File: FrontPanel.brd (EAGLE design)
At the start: 100 x 61 mm, 29 parts, among them U1 TPIC6B595N, U2 TPIC6B595N, U3 TPIC6B595N, U4 TPIC6B595N, U5 TPIC6B595N, U6 TPIC6B595N

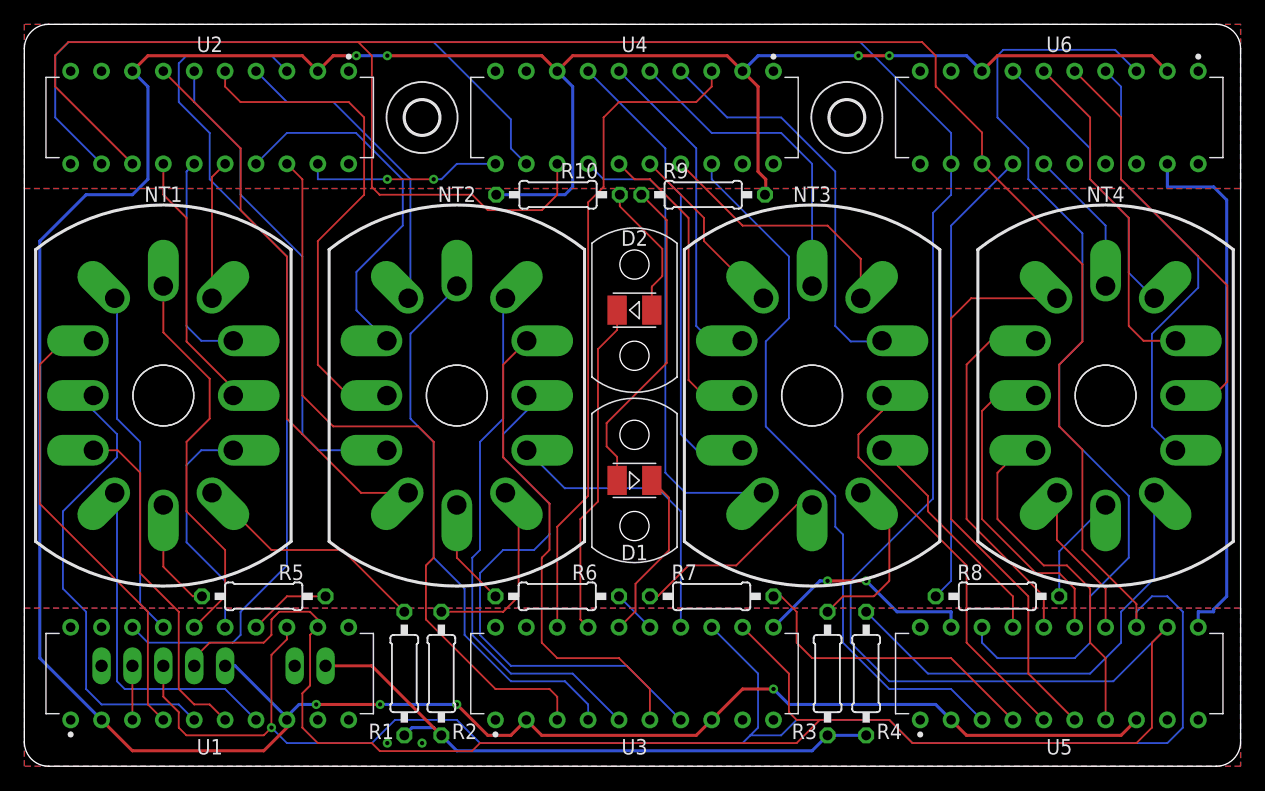
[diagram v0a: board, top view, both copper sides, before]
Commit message: added additional mounting hole
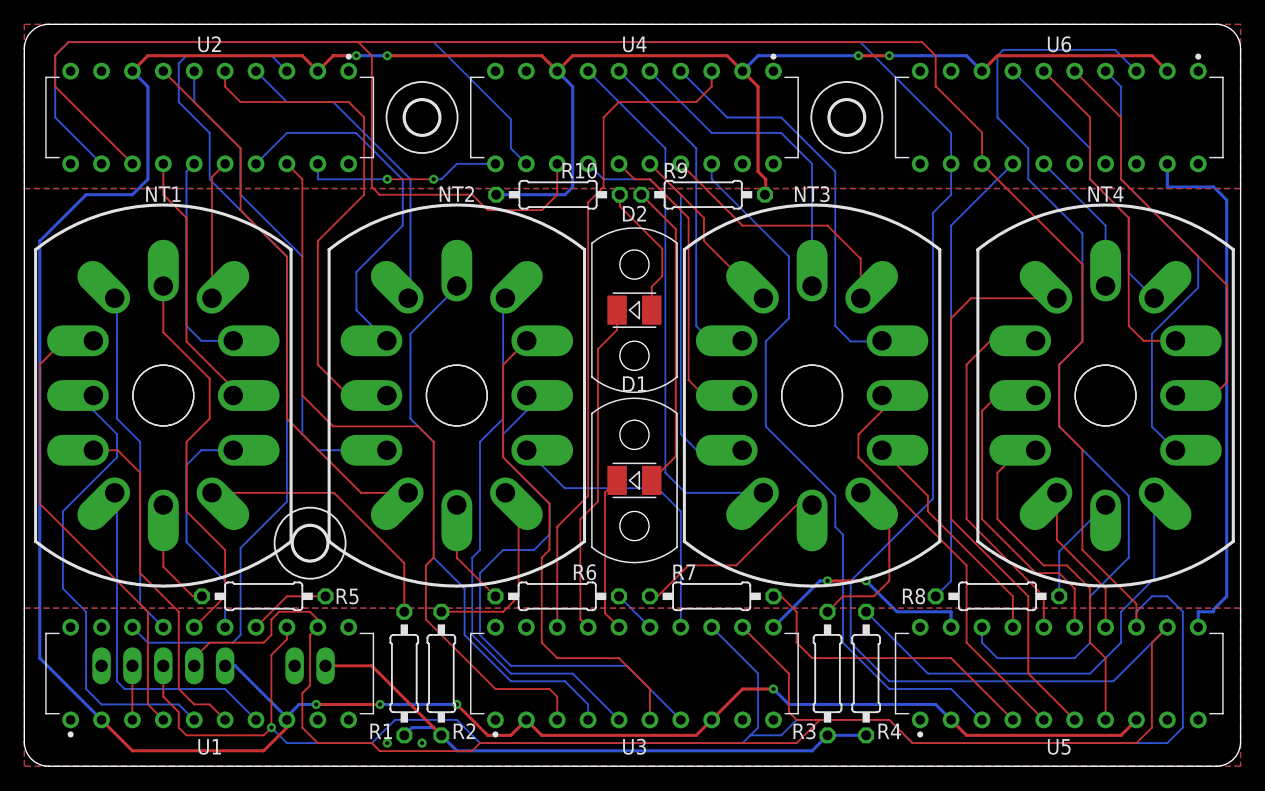
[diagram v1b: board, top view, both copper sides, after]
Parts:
- added U$3: (no value), holes:2,8
- turned D1 to 0 degrees
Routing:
- net N$49: track 19.9 -> 22.2 mm
- net LED1: track 14.4 -> 13.0 mm
- net N$66: track 26.8 -> 25.5 mm
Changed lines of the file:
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@@
 <drawing>
 <settings>
-<setting alwaysvectorfont="yes"/>
+<setting alwaysvectorfont="no"/>
 <setting verticaltext="up"/>
 </settings>
@@
 </element>
 <element name="R5" library="rcl" library_urn="urn:adsk.eagle:library:334" package="0207/10" package3d_urn="urn:adsk.eagle:package:23491/2" value="100k" x="19.685" y="13.97" smashed="yes">
-<attribute name="NAME" x="22.987" y="15.3162" size="1.27" layer="25" ratio="10" align="bottom-right"/>
+<attribute name="NAME" x="25.527" y="13.97" size="1.27" layer="25" ratio="10" align="center-left"/>
 <attribute name="SPICEPREFIX" value="R" x="38.735" y="-96.52" size="1.778" layer="27" display="off"/>
 <attribute name="VALUE" x="17.4244" y="13.335" size="1.27" layer="27" ratio="10"/>
@@
 </element>
 <element name="R8" library="rcl" library_urn="urn:adsk.eagle:library:334" package="0207/10" package3d_urn="urn:adsk.eagle:package:23491/2" value="100k" x="80.01" y="13.97" smashed="yes">
-<attribute name="NAME" x="76.708" y="15.3162" size="1.27" layer="25" ratio="10"/>
+<attribute name="NAME" x="74.168" y="13.97" size="1.27" layer="25" ratio="10" align="center-right"/>
 <attribute name="SPICEPREFIX" value="R" x="137.16" y="-96.52" size="1.778" layer="27" display="off"/>
 <attribute name="VALUE" x="77.7494" y="13.335" size="1.27" layer="27" ratio="10"/>
@@
 <element name="U$5" library="NixieClock" library_urn="urn:adsk.eagle:library:7479626" package="MENTOR-1216.1005" package3d_urn="urn:adsk.eagle:package:7524597/2" value="" x="50.165" y="37.5" smashed="yes" rot="R90"/>
 <element name="U$6" library="NixieClock" library_urn="urn:adsk.eagle:library:7479626" package="MENTOR-1216.1005" package3d_urn="urn:adsk.eagle:package:7524597/2" value="" x="50.165" y="23.5" smashed="yes" rot="R90"/>
-<element name="D1" library="Wurth_Elektronik_Optoelectronics_rev17b" library_urn="urn:adsk.eagle:library:446" package="WL-SMTW_3528" package3d_urn="urn:adsk.eagle:package:32264/1" value="" x="50.165" y="23.5" smashed="yes" rot="R180">
-<attribute name="COMPANY-URL" value="http://www.we-online.de" x="50.165" y="23.5" size="1.778" layer="27" rot="R180" display="off"/>
-<attribute name="CREATED-BY" value="Christin Otto" x="50.165" y="23.5" size="1.778" layer="27" rot="R180" display="off"/>
-<attribute name="CREATED-DATE" value="APR 2013" x="50.165" y="23.5" size="1.778" layer="27" rot="R180" display="off"/>
-<attribute name="DATASHEET-URL" value="http://katalog.we-online.de/en/led/WL-SMTW?m=t&amp;sq=smtw&amp;sp=&amp;sp=http%3A%2F%2Fwww.we-online.de%2Fweb%2Fen%2Felectronic_components%2Fsearchpage_PBS.php%3Fsearch%3Dsmtw" x="50.165" y="23.5" size="1.778" layer="27" rot="R180" display="off"/>
-<attribute name="MANUFACTURER" value="Würth Elektronik eiSos GmbH" x="50.165" y="23.5" size="1.778" layer="27" rot="R180" display="off"/>
-<attribute name="NAME" x="50.165" y="18.2095" size="1.27" layer="25" align="top-center"/>
-<attribute name="VALUE" x="52.305" y="26.31" size="0.8128" layer="27" rot="R180"/>
+<element name="D1" library="Wurth_Elektronik_Optoelectronics_rev17b" library_urn="urn:adsk.eagle:library:446" package="WL-SMTW_3528" package3d_urn="urn:adsk.eagle:package:32264/1" value="" x="50.165" y="23.5" smashed="yes">
+<attribute name="COMPANY-URL" value="http://www.we-online.de" x="50.165" y="23.5" size="1.778" layer="27" display="off"/>
+<attribute name="CREATED-BY" value="Christin Otto" x="50.165" y="23.5" size="1.778" layer="27" display="off"/>
+<attribute name="CREATED-DATE" value="APR 2013" x="50.165" y="23.5" size="1.778" layer="27" display="off"/>
+<attribute name="DATASHEET-URL" value="http://katalog.we-online.de/en/led/WL-SMTW?m=t&amp;sq=smtw&amp;sp=&amp;sp=http%3A%2F%2Fwww.we-online.de%2Fweb%2Fen%2Felectronic_components%2Fsearchpage_PBS.php%3Fsearch%3Dsmtw" x="50.165" y="23.5" size="1.778" layer="27" display="off"/>
+<attribute name="MANUFACTURER" value="Würth Elektronik eiSos GmbH" x="50.165" y="23.5" size="1.778" layer="27" display="off"/>
+<attribute name="NAME" x="50.165" y="30.7905" size="1.27" layer="25" rot="R180" align="top-center"/>
+<attribute name="VALUE" x="48.025" y="20.69" size="0.8128" layer="27"/>
 </element>
 <element name="D2" library="Wurth_Elektronik_Optoelectronics_rev17b" library_urn="urn:adsk.eagle:library:446" package="WL-SMTW_3528" package3d_urn="urn:adsk.eagle:package:32264/1" value="" x="50.165" y="37.5" smashed="yes">
@@
 <attribute name="DATASHEET-URL" value="http://katalog.we-online.de/en/led/WL-SMTW?m=t&amp;sq=smtw&amp;sp=&amp;sp=http%3A%2F%2Fwww.we-online.de%2Fweb%2Fen%2Felectronic_components%2Fsearchpage_PBS.php%3Fsearch%3Dsmtw" x="50.165" y="37.5" size="1.778" layer="27" display="off"/>
 <attribute name="MANUFACTURER" value="Würth Elektronik eiSos GmbH" x="50.165" y="37.5" size="1.778" layer="27" display="off"/>
-<attribute name="NAME" x="50.165" y="42.7905" size="1.27" layer="25" align="bottom-center"/>
+<attribute name="NAME" x="50.165" y="44.7905" size="1.27" layer="25" align="bottom-center"/>
 <attribute name="VALUE" x="48.025" y="34.69" size="0.8128" layer="27"/>
 </element>
+<element name="U$3" library="holes" library_urn="urn:adsk.eagle:library:237" package="2,8" package3d_urn="urn:adsk.eagle:package:14271/1" value="" x="23.495" y="18.34" smashed="yes"/>
 </elements>
 <signals>
@@
 <contactref element="U3" pad="16"/>
 <contactref element="D1" pad="1"/>
-<wire x1="50.25" y1="12.75" x2="50.25" y2="15" width="0.1524" layer="1"/>
-<wire x1="50.25" y1="15" x2="53" y2="17.75" width="0.1524" layer="1"/>
-<wire x1="53" y1="22.09" x2="51.59" y2="23.5" width="0.1524" layer="1"/>
-<wire x1="50.25" y1="12.75" x2="48.895" y2="11.395" width="0.1524" layer="1"/>
-<wire x1="48.895" y1="11.43" x2="48.895" y2="11.395" width="0.1524" layer="1"/>
-<wire x1="53" y1="17.75" x2="53" y2="22.09" width="0.1524" layer="1"/>
+<wire x1="48.74" y1="23.5" x2="47.74" y2="22.5" width="0.1524" layer="1"/>
+<wire x1="47.74" y1="22.5" x2="47.74" y2="12.585" width="0.1524" layer="1"/>
+<wire x1="47.74" y1="12.585" x2="48.895" y2="11.43" width="0.1524" layer="1"/>
 </signal>
 <signal name="LED2">
@@
 <contactref element="NT1" pad="A"/>
 <contactref element="R1" pad="1"/>
-<wire x1="31.242" y1="12.7" x2="26.162" y2="17.78" width="0.1524" layer="1"/>
-<wire x1="20.32" y1="17.78" x2="15.62" y2="22.48" width="0.1524" layer="1"/>
-<wire x1="15.62" y1="22.48" x2="15.43" y2="22.48" width="0.1524" layer="1"/>
-<wire x1="26.162" y1="17.78" x2="20.32" y2="17.78" width="0.1524" layer="1"/>
+<wire x1="31.242" y1="12.7" x2="31.242" y2="16.7" width="0.1524" layer="1"/>
+<wire x1="31.242" y1="16.7" x2="25.462" y2="22.48" width="0.1524" layer="1"/>
+<wire x1="25.462" y1="22.48" x2="15.43" y2="22.48" width="0.1524" layer="1"/>
 </signal>
 <signal name="N$50">
@@
 <contactref element="U2" pad="3"/>
 <contactref element="U1" pad="18"/>
-<wire x1="21.59" y1="16.51" x2="17.78" y2="12.7" width="0.1524" layer="16"/>
+<wire x1="21.59" y1="21.76" x2="17.78" y2="17.95" width="0.1524" layer="16"/>
 <wire x1="21.59" y1="41.91" x2="15.24" y2="48.26" width="0.1524" layer="16"/>
 <wire x1="15.24" y1="48.26" x2="15.24" y2="52.07" width="0.1524" layer="16"/>
 <wire x1="12.7" y1="54.61" x2="15.24" y2="52.07" width="0.1524" layer="16"/>
 <wire x1="21.59" y1="57.15" x2="20.32" y2="58.42" width="0.1524" layer="16"/>
-<wire x1="21.59" y1="16.51" x2="21.59" y2="41.91" width="0.1524" layer="16"/>
+<wire x1="21.59" y1="21.76" x2="21.59" y2="41.91" width="0.1524" layer="16"/>
 <wire x1="13.335" y1="58.42" x2="12.7" y2="57.785" width="0.1524" layer="16"/>
 <wire x1="12.7" y1="57.785" x2="12.7" y2="54.61" width="0.1524" layer="16"/>
@@
 <wire x1="17.78" y1="10.795" x2="17.145" y2="10.16" width="0.1524" layer="16"/>
 <wire x1="10.16" y1="10.16" x2="8.89" y2="11.43" width="0.1524" layer="16"/>
-<wire x1="17.78" y1="12.7" x2="17.78" y2="10.795" width="0.1524" layer="16"/>
+<wire x1="17.78" y1="17.95" x2="17.78" y2="10.795" width="0.1524" layer="16"/>
 <wire x1="17.145" y1="10.16" x2="10.16" y2="10.16" width="0.1524" layer="16"/>
 </signal>
@@
 <contactref element="R9" pad="1"/>
 <contactref element="D1" pad="2"/>
-<wire x1="48.74" y1="23.5" x2="48.74" y2="25.4333375" width="0.1524" layer="1"/>
-<wire x1="48.74" y1="25.4333375" x2="47.8728" y2="26.3005375" width="0.1524" layer="1"/>
-<wire x1="47.8728" y1="26.3005375" x2="47.8728" y2="28.2161375" width="0.1524" layer="1"/>
-<wire x1="52.8128" y1="44.9122" x2="52.8128" y2="33.1561375" width="0.1524" layer="1"/>
-<wire x1="50.735" y1="46.99" x2="52.8128" y2="44.9122" width="0.1524" layer="1"/>
-<wire x1="52.8128" y1="33.1561375" x2="47.8728" y2="28.2161375" width="0.1524" layer="1"/>
+<wire x1="53.5628" y1="44.1622" x2="53.5628" y2="25.4728" width="0.1524" layer="1"/>
+<wire x1="51.59" y1="23.5" x2="53.5628" y2="25.4728" width="0.1524" layer="1"/>
+<wire x1="50.735" y1="46.99" x2="53.5628" y2="44.1622" width="0.1524" layer="1"/>
 </signal>
 <signal name="N$67">

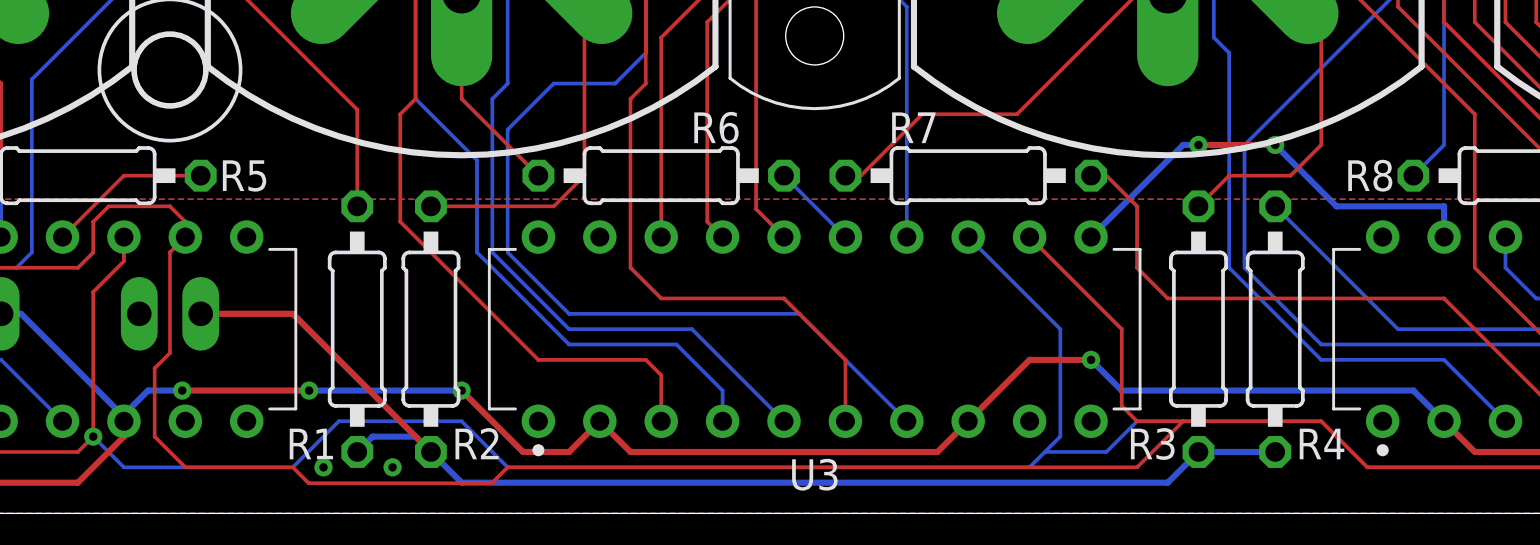
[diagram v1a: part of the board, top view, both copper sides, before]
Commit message: fixed airwire in front panel and updated panel
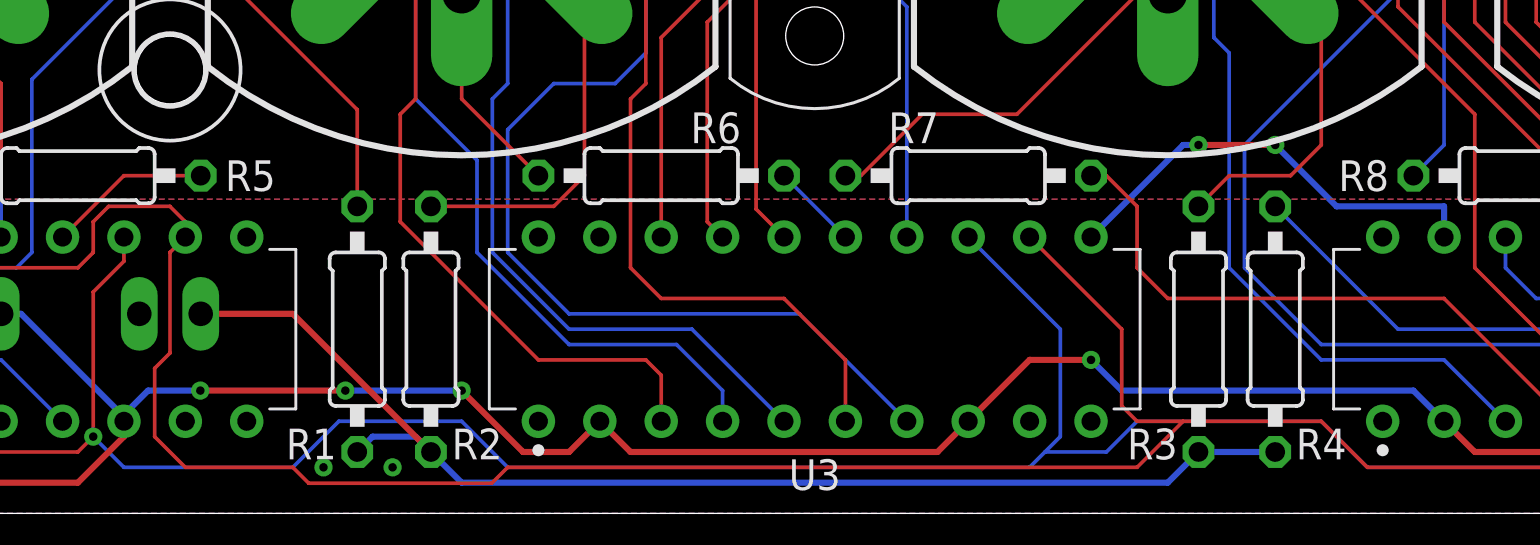
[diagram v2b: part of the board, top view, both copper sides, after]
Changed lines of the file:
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@@
 <drawing>
 <settings>
-<setting alwaysvectorfont="no"/>
+<setting alwaysvectorfont="yes"/>
 <setting verticaltext="up"/>
 </settings>
@@
 </element>
 <element name="R5" library="rcl" library_urn="urn:adsk.eagle:library:334" package="0207/10" package3d_urn="urn:adsk.eagle:package:23491/2" value="100k" x="19.685" y="13.97" smashed="yes">
-<attribute name="NAME" x="25.527" y="13.97" size="1.27" layer="25" ratio="10" align="center-left"/>
+<attribute name="NAME" x="25.777" y="13.97" size="1.27" layer="25" ratio="10" align="center-left"/>
 <attribute name="SPICEPREFIX" value="R" x="38.735" y="-96.52" size="1.778" layer="27" display="off"/>
 <attribute name="VALUE" x="17.4244" y="13.335" size="1.27" layer="27" ratio="10"/>
@@
 </element>
 <element name="R8" library="rcl" library_urn="urn:adsk.eagle:library:334" package="0207/10" package3d_urn="urn:adsk.eagle:package:23491/2" value="100k" x="80.01" y="13.97" smashed="yes">
-<attribute name="NAME" x="74.168" y="13.97" size="1.27" layer="25" ratio="10" align="center-right"/>
+<attribute name="NAME" x="73.918" y="13.97" size="1.27" layer="25" ratio="10" align="center-right"/>
 <attribute name="SPICEPREFIX" value="R" x="137.16" y="-96.52" size="1.778" layer="27" display="off"/>
 <attribute name="VALUE" x="77.7494" y="13.335" size="1.27" layer="27" ratio="10"/>
@@
 <wire x1="21.59" y1="3.81" x2="21.59" y2="4.08" width="0.254" layer="16"/>
 <wire x1="21.59" y1="4" x2="21.59" y2="3.81" width="0.254" layer="16"/>
-<wire x1="35.56" y1="5.08" x2="29.25" y2="5.08" width="0.254" layer="16"/>
 <wire x1="16.51" y1="8.255" x2="17.335" y2="8.255" width="0.254" layer="16"/>
 <wire x1="17.335" y1="8.255" x2="21.59" y2="4" width="0.254" layer="16"/>
-<via x="24" y="5.08" extent="1-16" drill="0.35" shape="octagon"/>
-<wire x1="22.59" y1="5.08" x2="24" y2="5.08" width="0.254" layer="16"/>
-<wire x1="24" y1="5.08" x2="29.25" y2="5.08" width="0.254" layer="1"/>
-<via x="29.25" y="5.08" extent="1-16" drill="0.35" shape="octagon"/>
 <wire x1="44.45" y1="46.99" x2="38.8" y2="46.99" width="0.254" layer="16"/>
 <wire x1="60.96" y1="48.26" x2="60.96" y2="47.055" width="0.254" layer="1"/>
 <wire x1="60.96" y1="47.055" x2="60.895" y2="46.99" width="0.254" layer="1"/>
+<via x="24.75" y="5.08" extent="1-16" drill="0.35" shape="octagon"/>
+<wire x1="22.59" y1="5.08" x2="24.75" y2="5.08" width="0.254" layer="16"/>
+<wire x1="24.75" y1="5.08" x2="30.74816875" y2="5.08" width="0.254" layer="1"/>
+<wire x1="30.74816875" y1="5.08" x2="30.749084375" y2="5.079084375" width="0.254" layer="1"/>
+<via x="30.749084375" y="5.079084375" extent="1-16" drill="0.35" shape="octagon"/>
+<wire x1="35.56" y1="5.08" x2="35.559084375" y2="5.079084375" width="0.254" layer="16"/>
+<wire x1="35.559084375" y1="5.079084375" x2="30.749084375" y2="5.079084375" width="0.254" layer="16"/>
 </signal>
 <signal name="SCLK">
